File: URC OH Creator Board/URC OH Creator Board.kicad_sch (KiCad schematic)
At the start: 20 parts, among them J1 Conn_01x20_Pin, J10 Conn_01x20_Pin, J11 Conn_01x20_Pin, J12 Conn_01x20_Pin, J2 Conn_01x20_Pin, J3 Conn_01x20_Pin, J4 Conn_01x20_Pin, J5 Conn_01x20_Pin, J6 Conn_01x20_Pin, J7 Conn_01x20_Pin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

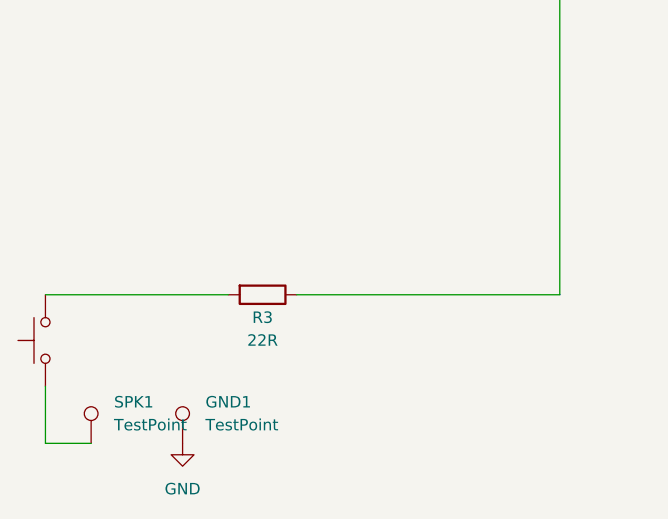
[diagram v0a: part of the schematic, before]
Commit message: Changed speaker series resistor to 10uF capacitor
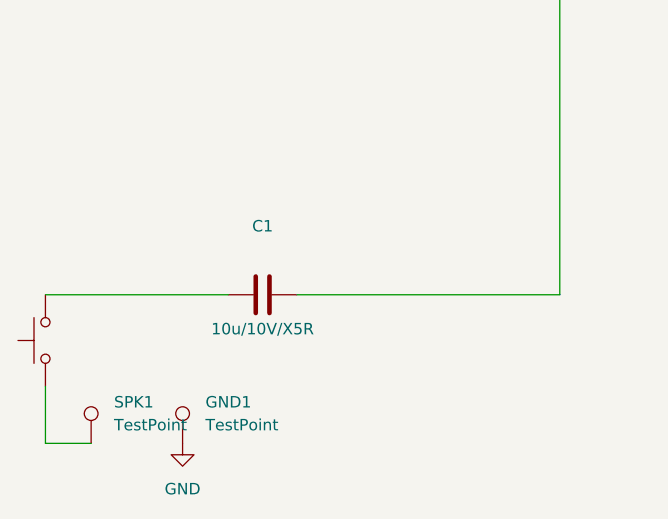
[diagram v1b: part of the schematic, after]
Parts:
- removed R3: 22R, Resistor_SMD:R_0603_1608Metric, symbol Device:R
- added C1: 10u/10V/X5R, Capacitor_SMD:C_0603_1608Metric, symbol Device:C
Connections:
- net RX Audio: now also C1.2
- net at SW2.2: now also C1.1
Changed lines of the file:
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@@
-    )
-  )
-  (symbol (lib_id "Device:R") (at 41.91 143.51 270) (unit 1)
-    (in_bom yes) (on_board yes) (dnp no)
-    (property "Reference" "R3" (at 41.91 146.05 90)
-      (effects (font (size 1.27 1.27)))
-    )
-    (property "Value" "22R" (at 41.91 148.59 90)
-      (effects (font (size 1.27 1.27)))
-    )
-    (property "Footprint" "Resistor_SMD:R_0603_1608Metric" (at 41.91 141.732 90)
-      (effects (font (size 1.27 1.27)) hide)
-    )
-    (property "Datasheet" "~" (at 41.91 143.51 0)
-      (effects (font (size 1.27 1.27)) hide)
-    )
-    (property "LCSC" "C23345" (at 41.91 146.05 0)
-      (effects (font (size 1.27 1.27)) hide)
-    )
-    (pin "1")
-    (pin "2")
-    (instances
-      (project "URC OH Creator Board"
-        (path "/2b50db3f-1cc8-4638-9e7a-621d12dd33f1"
-          (reference "R3") (unit 1)
-        )
-      )
-      (project "URCv2"
-        (path "/6b10ea87-c95d-4ec7-ad2b-5b0dcbbb7b7c"
-          (reference "R12") (unit 1)
-        )
-      )
     )
   )
@@
         )
       )
+    )
+  )
+  (symbol (lib_id "Device:C") (at 41.91 143.51 90) (unit 1)
+    (in_bom yes) (on_board yes) (dnp no)
+    (property "Reference" "C1" (at 41.91 135.89 90)
+      (effects (font (size 1.27 1.27)))
+    )
+    (property "Value" "10u/10V/X5R" (at 41.91 147.32 90)
+      (effects (font (size 1.27 1.27)))
+    )
+    (property "Footprint" "Capacitor_SMD:C_0603_1608Metric" (at 45.72 142.5448 0)
+      (effects (font (size 1.27 1.27)) hide)
+    )
+    (property "Datasheet" "~" (at 41.91 143.51 0)
+      (effects (font (size 1.27 1.27)) hide)
+    )
+    (property "LCSC" "C19702" (at 41.91 135.89 0)
+      (effects (font (size 1.27 1.27)) hide)
+    )
+    (pin "1")
+    (pin "2")
+    (instances
+      (project "URC OH Creator Board"
+        (path "/2b50db3f-1cc8-4638-9e7a-621d12dd33f1"
+          (reference "C1") (unit 1)
+        )
+      )
+      (project "URCv2"
+        (path "/6b10ea87-c95d-4ec7-ad2b-5b0dcbbb7b7c"
+          (reference "C25") (unit 1)
+        )
+      )
